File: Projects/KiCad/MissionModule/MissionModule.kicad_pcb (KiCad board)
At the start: 2 copper layers, 110 x 95 mm, 47 parts, among them J1 Conn_01x04_Pin, J2 Conn_01x04_Pin, J3 Micro_SD_Card_Det_Hirose_DM3AT, SW1 SW_Push, SW2 SW_Push, U2 ABX00012, U3 MCP2562-E-P, U4 TLP222A, U5 MCP2515-I/P, U6 MB85RS2MT, U7 MB85RS2MT, Y1 8MHz

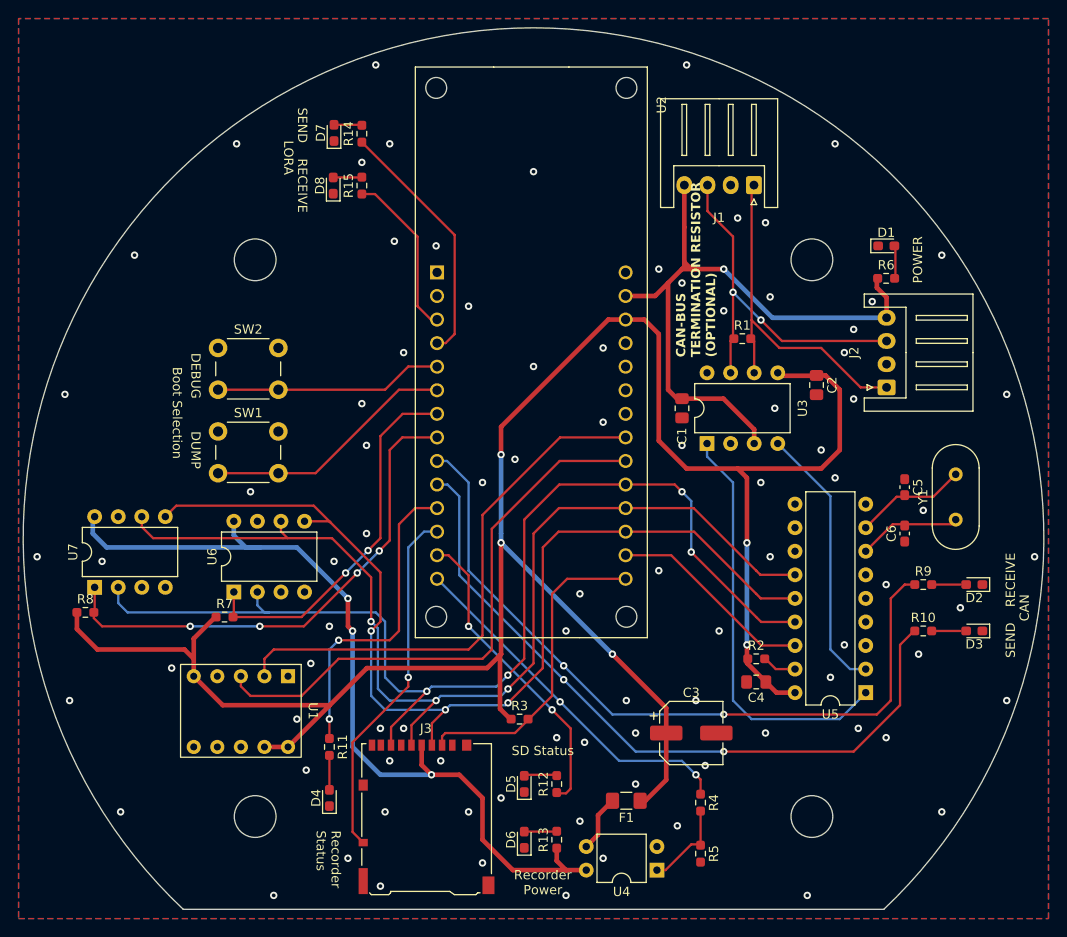
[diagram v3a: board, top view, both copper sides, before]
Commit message: コネクタを再配置, 基板上で12V->5Vをするように変更
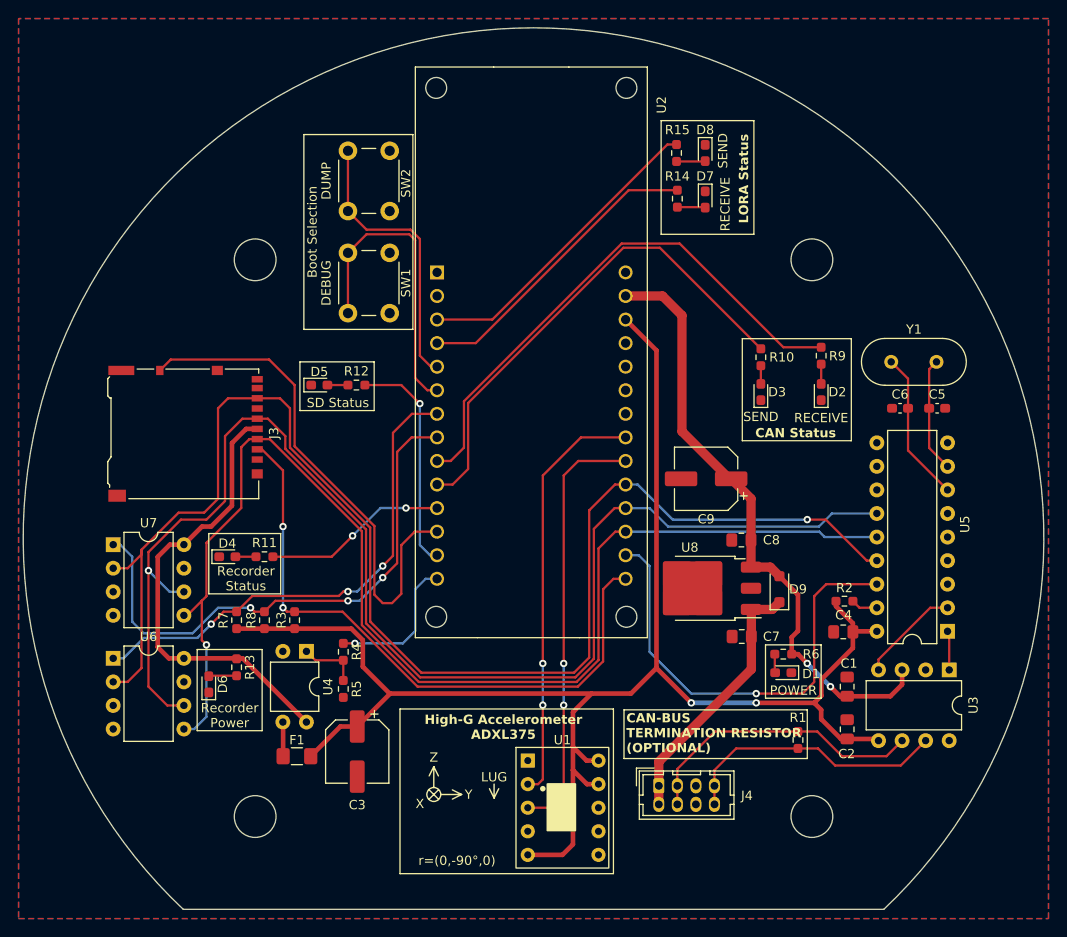
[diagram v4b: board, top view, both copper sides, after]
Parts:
- removed J1, J2: Conn_01x04_Pin, Connector_JST:JST_XH_S4B-XH-A_1x04_P2.50mm_Horizontal
- added C7: 0.33μF, Capacitor_SMD:C_0805_2012Metric_Pad1.18x1.45mm_HandSolder, F.Cu at (170.9, 115.6)
- added C8: 0.1μF, Capacitor_SMD:C_0805_2012Metric_Pad1.18x1.45mm_HandSolder, F.Cu at (170.9, 105.2)
- added C9: 100μF, Capacitor_SMD:CP_Elec_6.3x7.7, F.Cu at (167.1, 98.6)
- added D9: 1N4007, Diode_SMD:D_SOD-123F, F.Cu at (175.0, 110.5)
- added J4: Conn_01x08, Connector_Hirose:Hirose_DF11-8DP-2DSA_2x04_P2.00mm_Vertical, F.Cu at (162.0, 131.7)
- added U8: NJM7805SDL1, Package_TO_SOT_SMD:TO-252-3_TabPin2, F.Cu at (166.9, 110.4)
- moved J3 48.8 mm to (111.0, 93.8), turned to -90 degrees
- moved D5 48.3 mm to (125.4, 88.5), turned to 0 degrees
- moved R12 48.1 mm to (129.4, 88.5), turned to 180 degrees
- moved D1 47.3 mm to (175.4, 119.5), turned to 180 degrees
- moved U4 44.5 mm to (124.0, 117.2), turned to -90 degrees
- moved R1 43.7 mm to (177.0, 126.8), turned to 90 degrees
- moved R5 42.4 mm to (128.0, 121.2)
- moved R6 42.0 mm to (175.4, 117.5), turned to 180 degrees
- moved R4 41.8 mm to (128.0, 117.2)
- moved D7 40.6 mm to (167.0, 68.5), turned to -90 degrees
- moved D8 40.2 mm to (167.0, 63.5), turned to -90 degrees
- moved R13 39.2 mm to (116.5, 118.9), turned to -90 degrees
- moved D6 37.9 mm to (113.5, 120.8)
- moved C2 37.2 mm to (182.3, 125.6), turned to 90 degrees
- moved C3 36.1 mm to (129.5, 128.0), turned to -90 degrees
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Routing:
- net +3.3V: track 234.7 -> 174.0 mm, vias 5 -> 2
- net MEMORY_POWER: track 93.0 -> 49.5 mm, vias 3 -> 0
- net CAN_TX: track 45.2 -> 4.23 mm
- net SPI_SCLK: track 113.7 -> 147.9 mm, vias 3 -> 1
- net SPI_MISO: track 119.9 -> 154.0 mm, vias 4 -> 1
- net SPI_CS_SD: track 34.2 -> 68.3 mm, vias 0 -> 2
- net +12V: track 0.00 -> 28.5 mm
- net SPI_CS_MCP: track 22.3 -> 49.0 mm, vias 0 -> 1
- net SPI_MOSI: track 112.5 -> 136.2 mm, vias 3 -> 1
- net CAN_SEND_STATUS: track 77.5 -> 54.1 mm, vias 2 -> 0
- net MEMORY_POWER_CONTROL: track 38.9 -> 15.6 mm, vias 2 -> 1
- net CAN_RECEIVE_STATUS: track 80.5 -> 58.7 mm, vias 2 -> 0
- net CAN_RX: track 29.2 -> 10.9 mm
- net SD_CHECK: track 38.6 -> 55.7 mm, vias 1 -> 0
- net LORA_SEND_STATUS: track 18.1 -> 33.6 mm
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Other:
- board text added: "CAN Status"
- board text added: "High-G Accelerometer ADXL375"
- board text added: "LORA Status"
- board text added: "LUG"
- board text added: "X"
- board text added: "Y"
- board text added: "Z"
- board text added: "r=(0,-90°,0)"
- board text removed: "CAN"
- board text removed: "LORA"

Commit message: 基板設計の都市伝説をいろいろ適応
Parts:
- REF** (x4): value MountingHole_4.5mm -> MountingHole_4.5mm_Pad_Via; footprint MountingHole:MountingHole_4.5mm -> MountingHole:MountingHole_4.5mm_Pad_Via
- moved R1 17.0 mm to (193.9, 129.0), turned to 0 degrees
- renumbered C5 to C1, C1 to C2, C7 to C3, C2 to C4, C4 to C5, C8 to C7, C9 to C8, C3 to C9, D9 to D2, D2 to D3, D3 to D4, D7 to D5, D8 to D6, D4 to D7, D5 to D8, D6 to D9, J4 to J1, J3 to J2, R4 to R10, R3 to R12, R8 to R13, R7 to R14, R12 to R15, R6 to R2, R2 to R3, R9 to R4, R10 to R5, R14 to R6, R15 to R7, R5 to R8, R13 to R9, U3 to U1, U5 to U2, U8 to U3, U1 to U4, U4 to U5, U2 to U6, U6 to U7, U7 to U8
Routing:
- net CAN_L: track 31.5 -> 43.4 mm
- net CAN_H: track 29.3 -> 39.7 mm
- net +3.3V: track 174.0 -> 176.5 mm, vias 2 -> 4
- net +5V: track 66.1 -> 67.5 mm, vias 2 -> 4
- net CAN_RECEIVE_STATUS: track 58.7 -> 57.9 mm
- net SPI_CS_SD: track 68.3 -> 67.6 mm
- net GND: vias 0 -> 187
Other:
- board text added: "CAN-BUS Termination Resistor"
- board text added: "Lug"
- board text removed: "CAN-BUS TERMINATION RESISTOR (OPTIONAL)"
- board text removed: "LUG"

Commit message: 裏面にQRコードと署名を追加
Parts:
- added G***: LOGO, LOGO, B.Cu at (147.0, 74.0)
- added G***: LOGO, LOGO, B.Cu at (148.5, 63.0)
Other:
- board text added: "Designed by Y.Iwai 2023"
- board text added: "Mission Module Build 1"
- board text added: "Tokai Student Rocket Poject H-58 Avionics"

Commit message: コネクタ類の3Dモデルを追加
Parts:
- J1: footprint Connector_Hirose:Hirose_DF11-8DP-2DSA_2x04_P2.00mm_Vertical -> Hirose_Connector:Hirose_DF11B-8DP-2DS
